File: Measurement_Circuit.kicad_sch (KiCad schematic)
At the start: 52 parts, among them IC1 ISO6721RBDR, J7 Screw_Terminal_01x02, J8 Screw_Terminal_01x03, J9 Screw_Terminal_01x03, U7 ADE7953xCP, U8 ISO1541, Y2 3.58 MHz

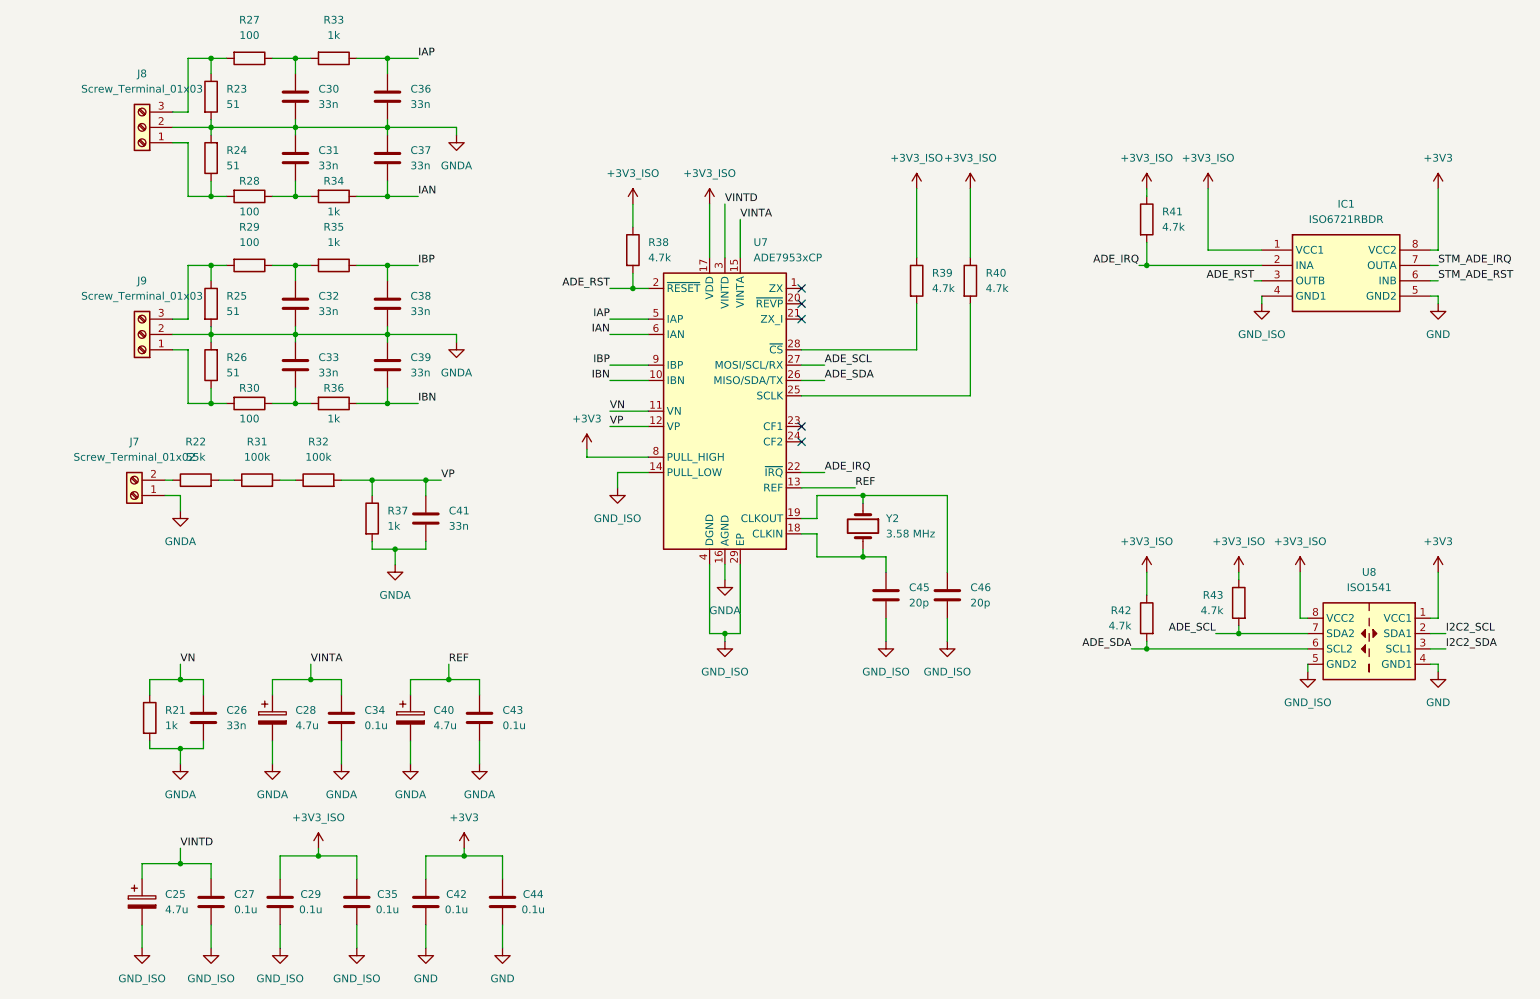
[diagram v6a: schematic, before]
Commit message: Footprints and elements update
Added another batch of footprints and links to the elements. More coming soon.
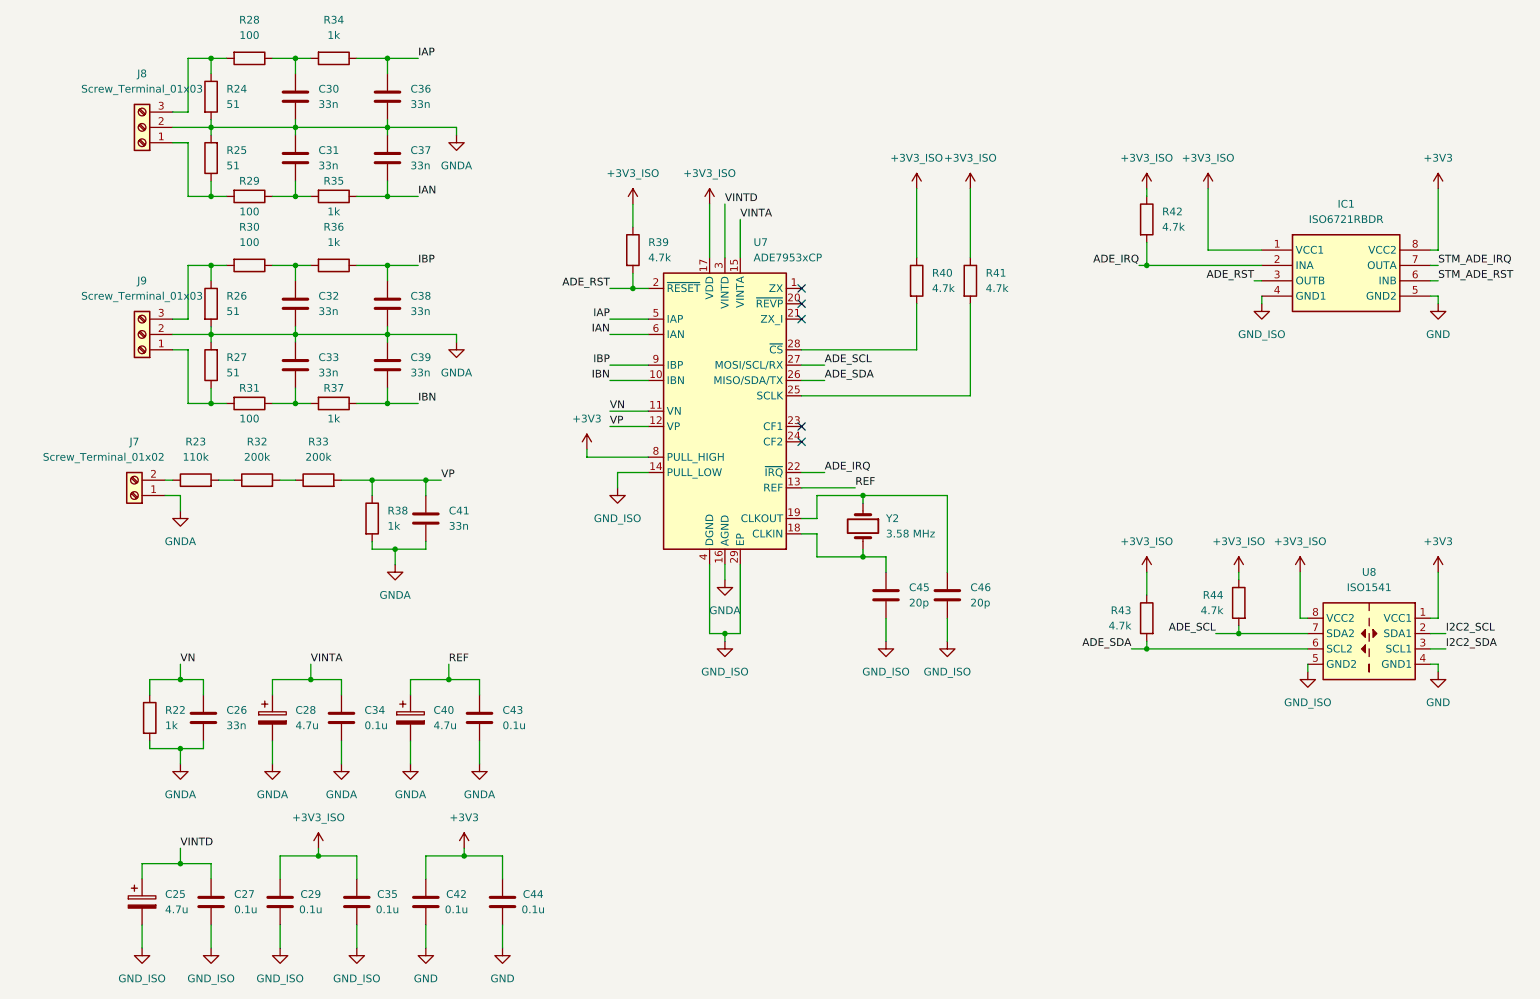
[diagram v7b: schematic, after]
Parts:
- C27, C29, C34, C35, C42, C43, C44: footprint Capacitor_SMD:C_0201_0603Metric_Pad0.64x0.40mm_HandSolder -> Capacitor_SMD:C_0603_1608Metric_Pad1.08x0.95mm_HandSolder
- R22: renamed from R21; footprint (none) -> Resistor_SMD:R_0603_1608Metric_Pad0.98x0.95mm_HandSolder
- R23: renamed from R22; value 55k -> 110k
- R32: renamed from R31; value 100k -> 200k
- R33: renamed from R32; value 100k -> 200k
- R39: renamed from R38; footprint (none) -> Resistor_SMD:R_0603_1608Metric_Pad0.98x0.95mm_HandSolder
- R40: renamed from R39; footprint (none) -> Resistor_SMD:R_0603_1608Metric_Pad0.98x0.95mm_HandSolder
- R41: renamed from R40; footprint (none) -> Resistor_SMD:R_0603_1608Metric_Pad0.98x0.95mm_HandSolder
- R42: renamed from R41; footprint (none) -> Resistor_SMD:R_0603_1608Metric_Pad0.98x0.95mm_HandSolder
- R43: renamed from R42; footprint (none) -> Resistor_SMD:R_0603_1608Metric_Pad0.98x0.95mm_HandSolder
- R44: renamed from R43; footprint (none) -> Resistor_SMD:R_0603_1608Metric_Pad0.98x0.95mm_HandSolder
- renumbered R23 to R24, R24 to R25, R25 to R26, R26 to R27, R27 to R28, R28 to R29, R29 to R30, R30 to R31, R33 to R34, R34 to R35, R35 to R36, R36 to R37, R37 to R38

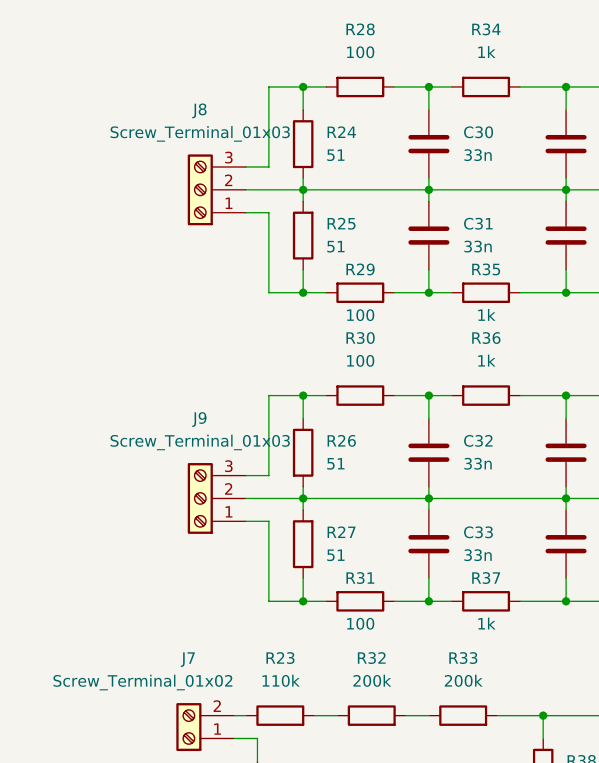
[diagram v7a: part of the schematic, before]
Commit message: 1st complete version of schematic with footprints
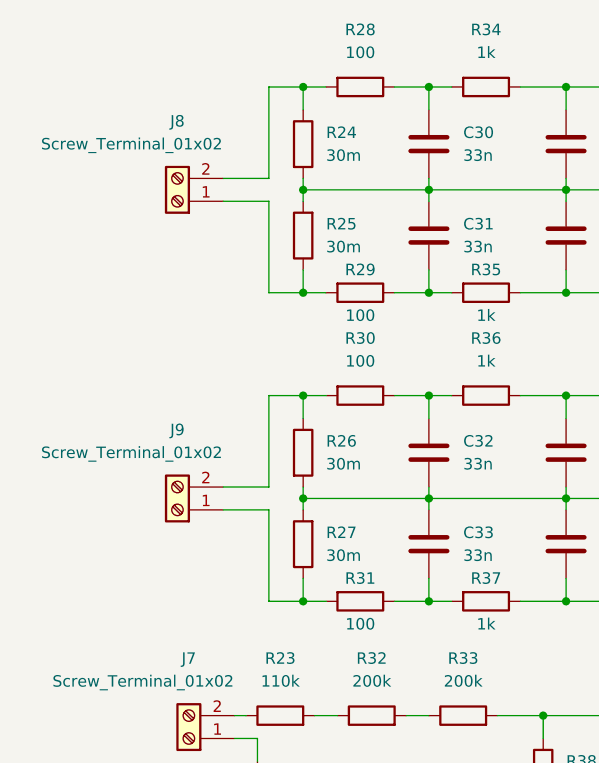
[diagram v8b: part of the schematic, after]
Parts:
- removed J8, J9: Screw_Terminal_01x03, symbol Connector:Screw_Terminal_01x03
- added J8, J9: Screw_Terminal_01x02, LibLoader:TB508P2PBL, symbol Connector:Screw_Terminal_01x02
- C41: footprint Capacitor_SMD:C_0603_1608Metric_Pad1.08x0.95mm_HandSolder -> Capacitor_SMD:C_1210_3225Metric_Pad1.33x2.70mm_HandSolder
- J7: footprint (none) -> LibLoader:TB508P2PBL
- R23, R28, R29, R30, R31, R32, R33, R34, R35, R36, R37, R38: footprint (none) -> Resistor_SMD:R_0805_2012Metric_Pad1.20x1.40mm_HandSolder
- R24, R25, R26, R27: value 51 -> 30m; footprint (none) -> Resistor_SMD:R_2512_6332Metric_Pad1.40x3.35mm_HandSolder
- Y2: footprint (none) -> Crystal:Crystal_SMD_HC49-SD_HandSoldering
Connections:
- net at R27.1, R31.2: now also J9.1 (Pin_1)
- net at R26.1, R30.2: now also J9.2 (Pin_2)
- net at R25.1, R29.2: now also J8.1 (Pin_1)
- net at R24.1, R28.2: now also J8.2 (Pin_2)
